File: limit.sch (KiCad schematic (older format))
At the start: 4 parts, among them P0 GP1S093HCZ0F

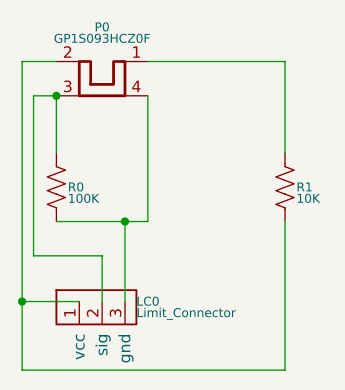
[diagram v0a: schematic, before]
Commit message: resistance changed from 10K to 1K ohms
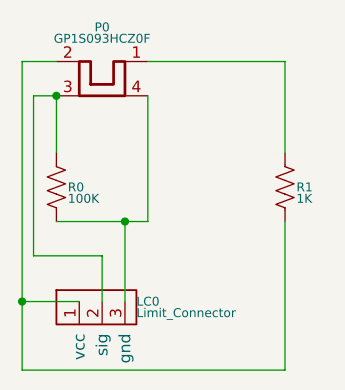
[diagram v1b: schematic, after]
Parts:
- R1: value 10K -> 1K
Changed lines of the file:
@@
 P 6750 3450
 F 0 "R1" H 6800 3450 39  0000 L CNN
-F 1 "10K" H 6800 3400 39  0000 L CNN
+F 1 "1K" H 6800 3400 39  0000 L CNN
 F 2 "Resistor_THT:R_Axial_DIN0207_L6.3mm_D2.5mm_P7.62mm_Horizontal" V 6790 3440 50  0001 C CNN
 F 3 "~" H 6750 3450 50  0001 C CNN
